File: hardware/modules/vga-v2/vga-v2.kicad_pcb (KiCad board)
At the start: 2 copper layers, 75 x 100 mm, 68 parts, among them J201 Conn_02x12_Male, J301 Conn_02x05_Odd_Even, J401 DB15_Female_HighDensity_Mount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, SW301 SW_Push, U201 11AA020, U202 74LVC4245, U203 4050, U204 MIC5504-1.2YM5, U205 LDL1117, U301 W25Q32JVSS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

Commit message: Use existing button
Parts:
- SW301: footprint Button_Switch_THT:SW_TH_Tactile_Omron_B3F-10xx -> Button_Switch_THT:SW_PUSH_6mm_H5mm
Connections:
- SW301 pad 2: Net-(C314-Pad1) -> GND
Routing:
- net GND: vias 128 -> 131
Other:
- board text added: "DONE"
- board text added: "RESET"

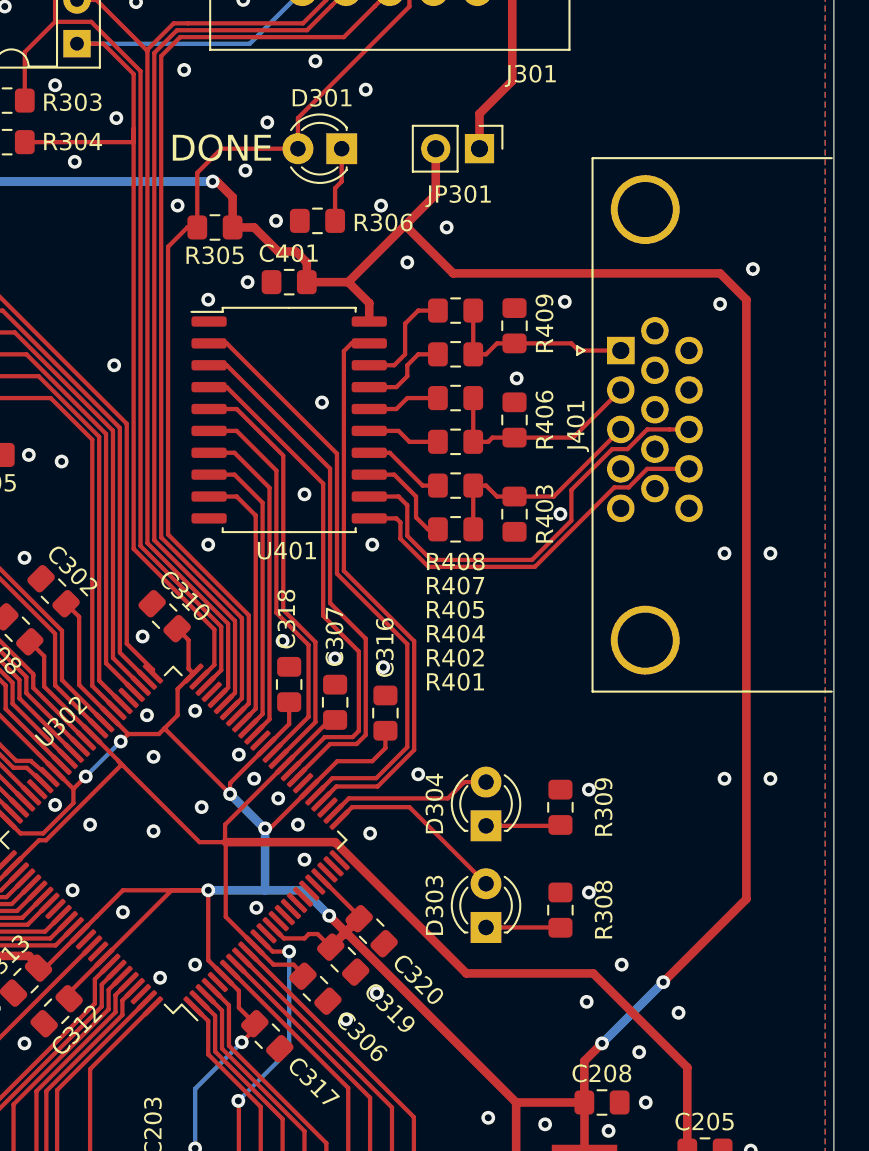
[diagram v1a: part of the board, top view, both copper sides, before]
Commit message: VGA Module V2 Production Files
Various changes, including: Smaller VGA connector, fix soldermask
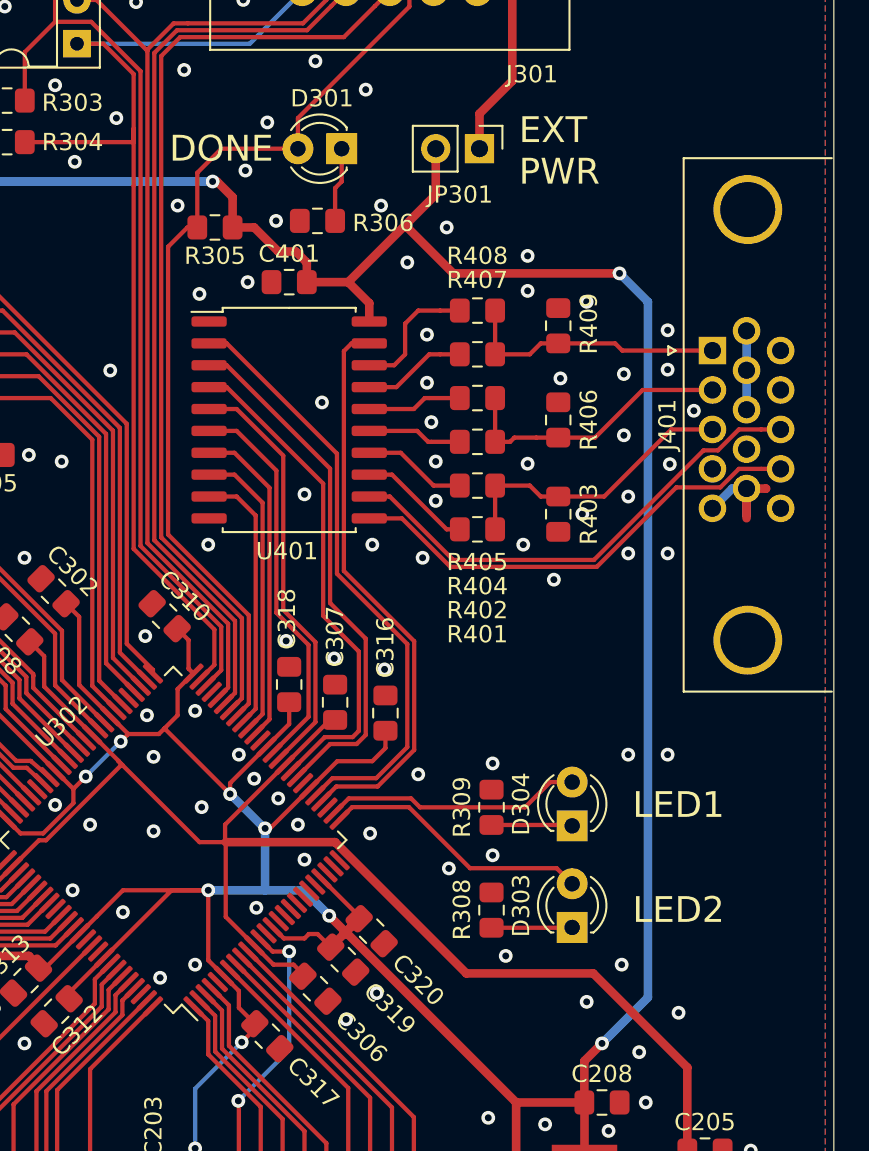
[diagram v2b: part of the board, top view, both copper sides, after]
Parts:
- J401: footprint Connector_Dsub:DSUB-15-HD_Female_Horizontal_P2.29x1.98mm_EdgePinOffset8.35mm_Housed_MountingHolesOffset10.89mm -> Connector_Dsub:DSUB-15-HD_Female_Horizontal_P2.29x1.98mm_EdgePinOffset3.03mm_Housed_MountingHolesOffset4.94mm
- moved J401 5.32 mm to (220.3, 70.9)
- moved D303 5.00 mm to (212.1, 104.4)
- moved D304 5.00 mm to (212.1, 98.5)
- moved R308 4.00 mm to (207.4, 103.4)
- moved R309 4.00 mm to (207.4, 97.4)
- moved R403 2.54 mm to (211.3, 80.4)
- moved R406 2.54 mm to (211.3, 74.9)
- moved R409 2.54 mm to (211.3, 69.5)
- moved R401 1.27 mm to (206.6, 81.3)
- moved R402 1.27 mm to (206.6, 78.7)
- moved R404 1.27 mm to (206.6, 76.2)
- moved R405 1.27 mm to (206.6, 73.7)
- moved R407 1.27 mm to (206.6, 71.1)
- moved R408 1.27 mm to (206.6, 68.6)
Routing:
- net GND: track 0.00 -> 11.5 mm, vias 131 -> 154
- net +3V3: track 406.9 -> 398.7 mm
- net Net-(D304-Pad2): track 9.61 -> 15.0 mm
- net Net-(D303-Pad2): track 10.6 -> 15.6 mm
- net /Output/~VSYNC_OUT: track 22.6 -> 27.4 mm
- net /Output/RED: track 11.5 -> 15.6 mm
- net /Output/BLUE: track 13.0 -> 17.0 mm
- net /Output/GREEN: track 12.4 -> 16.4 mm
- net /Output/~HSYNC_OUT: track 25.3 -> 28.5 mm
- net Net-(R408-Pad1): track 6.34 -> 7.61 mm
- net Net-(R404-Pad1): track 4.25 -> 5.52 mm
- net Net-(R402-Pad1): track 4.78 -> 6.05 mm
- net Net-(R405-Pad1): track 4.25 -> 5.52 mm
- net Net-(R407-Pad1): track 5.15 -> 6.05 mm
- net Net-(R401-Pad1): track 6.01 -> 6.57 mm
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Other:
- rule solder_mask_min_width: 0.25 -> 0.2
- board text added: "EXT PWR"
- board text added: "LED1"
- board text added: "LED2"
